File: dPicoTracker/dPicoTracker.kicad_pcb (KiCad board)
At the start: 2 copper layers, 32 x 76.1 mm, 43 parts, among them IC1 ATGM336H-5N31, J1 Conn_01x02_Pin, Q1 AO3401A, Q2 AO3401A, U3 CJ431, U4 CJ431, U5 TPS61221DCK, U7 MAX809STRG, U8 BMP280, Y1 Si5351A-B-GT, Y2 XOS25026000LT00351005

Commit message: rf tune
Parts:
- moved AE3 2.01 mm to (46.1, 77.9)
- moved IC1 1.82 mm to (59.0, 81.2)
- moved R9 1.45 mm to (60.2, 93.2)
- moved C19 1.03 mm to (63.8, 89.8)
- moved Q2 1.00 mm to (60.5, 89.4)
- moved U7 0.71 mm to (54.4, 94.2)
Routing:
- net /GPS_1PPS: track 40.2 -> 0.00 mm
- net +3V3: track 140.9 -> 121.9 mm
- net Net-(IC1-VCC): track 16.9 -> 0.00 mm, vias 2 -> 0
- net /UART1_RX: track 15.5 -> 0.00 mm
- net /UART1_TX: track 14.1 -> 0.00 mm
- net /GPS_RESET: track 13.9 -> 0.00 mm, vias 1 -> 0
- net /GPS_ON: track 12.3 -> 0.00 mm
- net /RESET: track 2.29 -> 0.00 mm
- net GND: track 44.0 -> 41.9 mm, vias 11 -> 41
- net /GPS_PWR_T: track 31.3 -> 29.7 mm
- net Net-(AE3-A): track 9.02 -> 8.00 mm

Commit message: pcb v1
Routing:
- net /GPS_1PPS: track 0.00 -> 37.9 mm
- net +3V3: track 121.9 -> 152.2 mm
- net Net-(IC1-VCC): track 0.00 -> 16.4 mm, vias 0 -> 2
- net /UART1_RX: track 0.00 -> 14.9 mm
- net GND: track 41.9 -> 55.5 mm
- net /UART1_TX: track 0.00 -> 13.4 mm
- net /GPS_ON: track 0.00 -> 10.5 mm
- net /GPS_RESET: track 0.00 -> 9.87 mm
- net /RESET: track 0.00 -> 2.48 mm

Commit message: finishing touches
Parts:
- added C1: 100nF, Capacitor_SMD:C_1206_3216Metric, F.Cu at (61.1, 117.0)
- added J2: Conn_01x05_Pin, Connector_PinSocket_2.54mm:PinSocket_1x05_P2.54mm_Vertical, F.Cu at (54.0, 112.0)
- C11, C13: value 240pF -> 180pF
- C12: value 430pF -> 300pF
- C14, C16: value 24pF -> 18pF
- C15: value 43pF -> 30pF
- L2, L3: value 750nH -> 560nH
- L4, L5: value 75nH -> 56nH
- Y2: value XOS25026000LT00351005 -> C132296
- moved Q1 1.07 mm to (61.2, 113.7)
- moved C5 0.08 mm to (58.1, 101.8)
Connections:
- A1 pad 24: unconnected-(A1-GPIO18-Pad24) -> Net-(A1-GPIO18)
- A1 pad 25: unconnected-(A1-GPIO19-Pad25) -> Net-(A1-GPIO19)
- A1 pad 26: unconnected-(A1-GPIO20-Pad26) -> Net-(A1-GPIO20)
- A1 pad 27: unconnected-(A1-GPIO21-Pad27) -> Net-(A1-GPIO21)
- A1 pad 29: unconnected-(A1-GPIO22-Pad29) -> Net-(A1-GPIO22)
- Y1 pad 2: /VFO_OSC -> Net-(Y1-XA)
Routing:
- net Net-(A1-GPIO22): track 0.00 -> 6.01 mm
- net GND: track 55.5 -> 60.8 mm
- net /VFO_OSC: track 6.39 -> 2.04 mm
- net Net-(A1-GPIO21): track 0.00 -> 3.72 mm
- net Net-(A1-GPIO20): track 0.00 -> 3.72 mm
- net Net-(A1-GPIO19): track 0.00 -> 3.72 mm
- net Net-(A1-GPIO18): track 0.00 -> 3.72 mm
- net Net-(Y1-XA): track 0.00 -> 2.88 mm
- net /VFO_3v3: track 33.7 -> 31.2 mm, vias 2 -> 0
- net /VFO_SCL: track 18.0 -> 19.3 mm
- net /GPS_1PPS: track 37.9 -> 39.1 mm
- net +3V3: track 152.2 -> 151.2 mm
- net /VFO_PWR_T: track 35.9 -> 34.8 mm
- net /VFO_SDA: track 23.4 -> 23.1 mm, vias 0 -> 1
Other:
- board text added: "18"
- board text added: "19"
- board text added: "20"
- board text added: "21"
- board text added: "22"
- board text added: "Designed for Apex 2025"
- board text added: "Dual Band Pico Tracker v1.3"
- board text added: "Marcus Kauffman KN6UYL Joshua Truman Hudson Hilal"

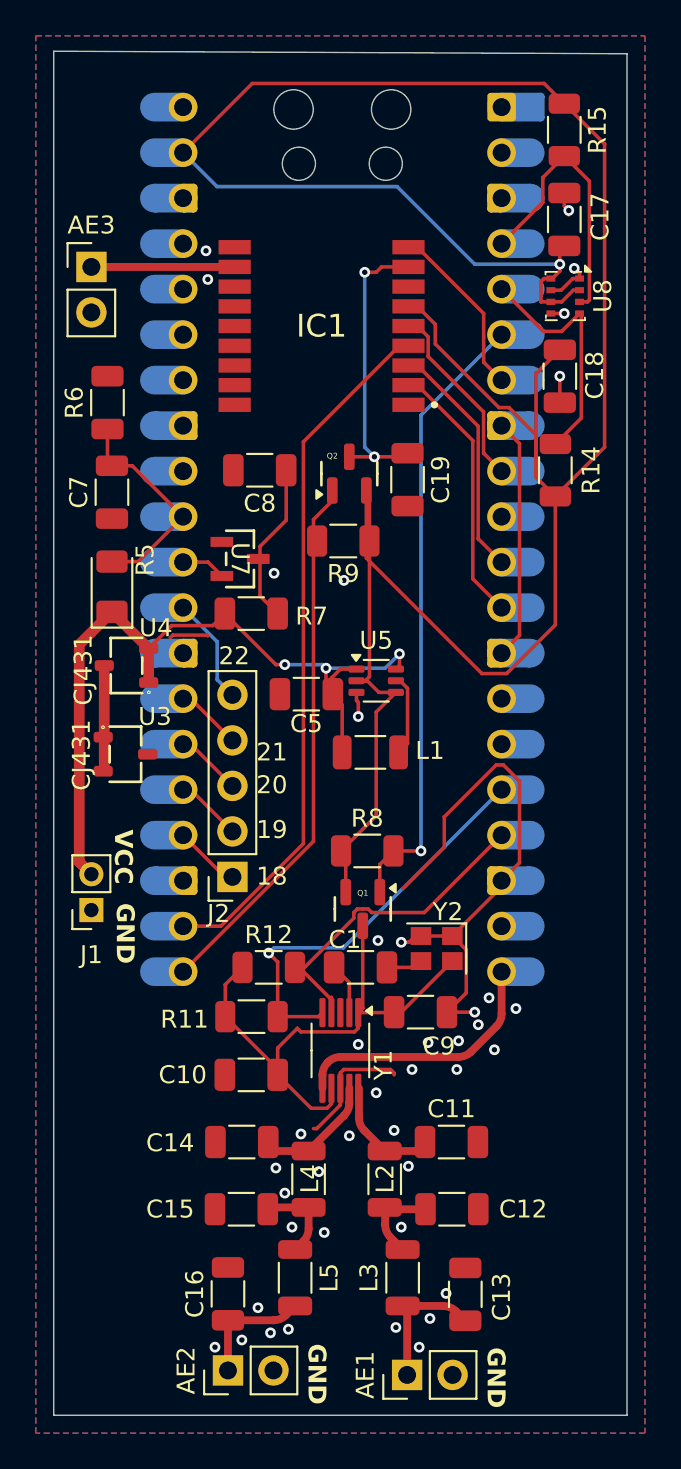
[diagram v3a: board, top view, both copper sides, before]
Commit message: finish tracker with dedicated RF
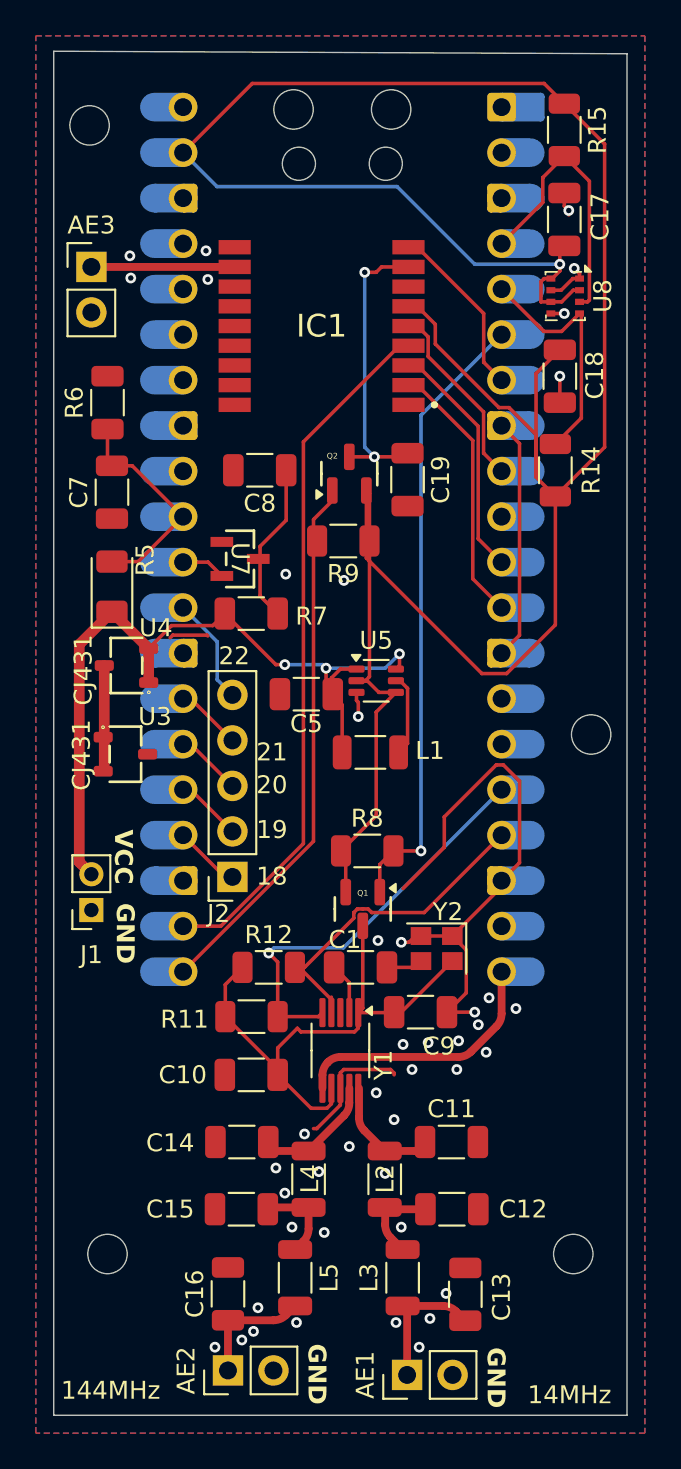
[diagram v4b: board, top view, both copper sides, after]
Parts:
- added REF**: MountingHole_2.2mm_M2, MountingHole:MountingHole_2.2mm_M2, F.Cu at (47.0, 133.0)
- added REF**: MountingHole_2.2mm_M2, MountingHole:MountingHole_2.2mm_M2, F.Cu at (73.0, 133.0)
- added REF**: MountingHole_2.2mm_M2, MountingHole:MountingHole_2.2mm_M2, F.Cu at (46.0, 70.0)
- added REF**: MountingHole_2.2mm_M2, MountingHole:MountingHole_2.2mm_M2, F.Cu at (74.0, 104.0)
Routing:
- net GND: vias 41 -> 43
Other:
- board text added: "144MHz"
- board text added: "14MHz"
